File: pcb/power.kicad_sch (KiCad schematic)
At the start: 38 parts, among them U10 TPS541620

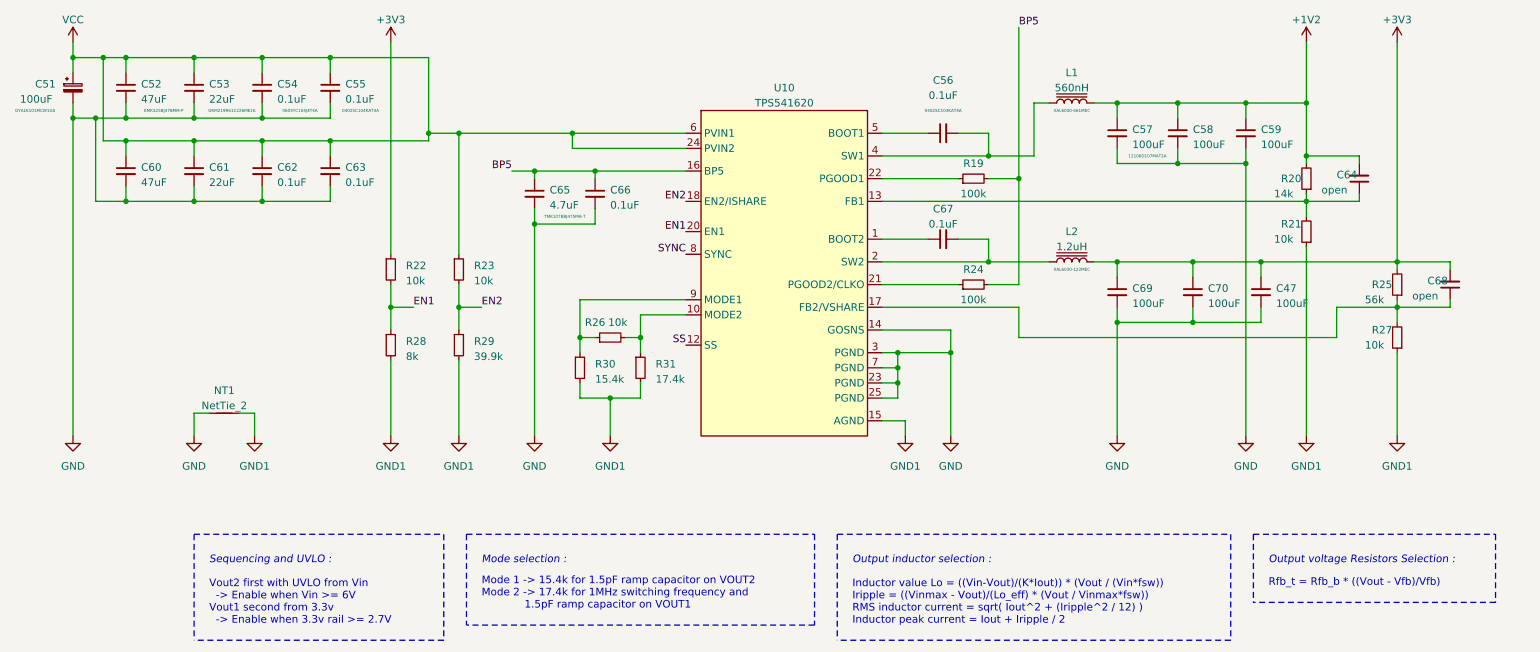
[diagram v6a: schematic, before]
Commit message: change to lx9 and reduce power
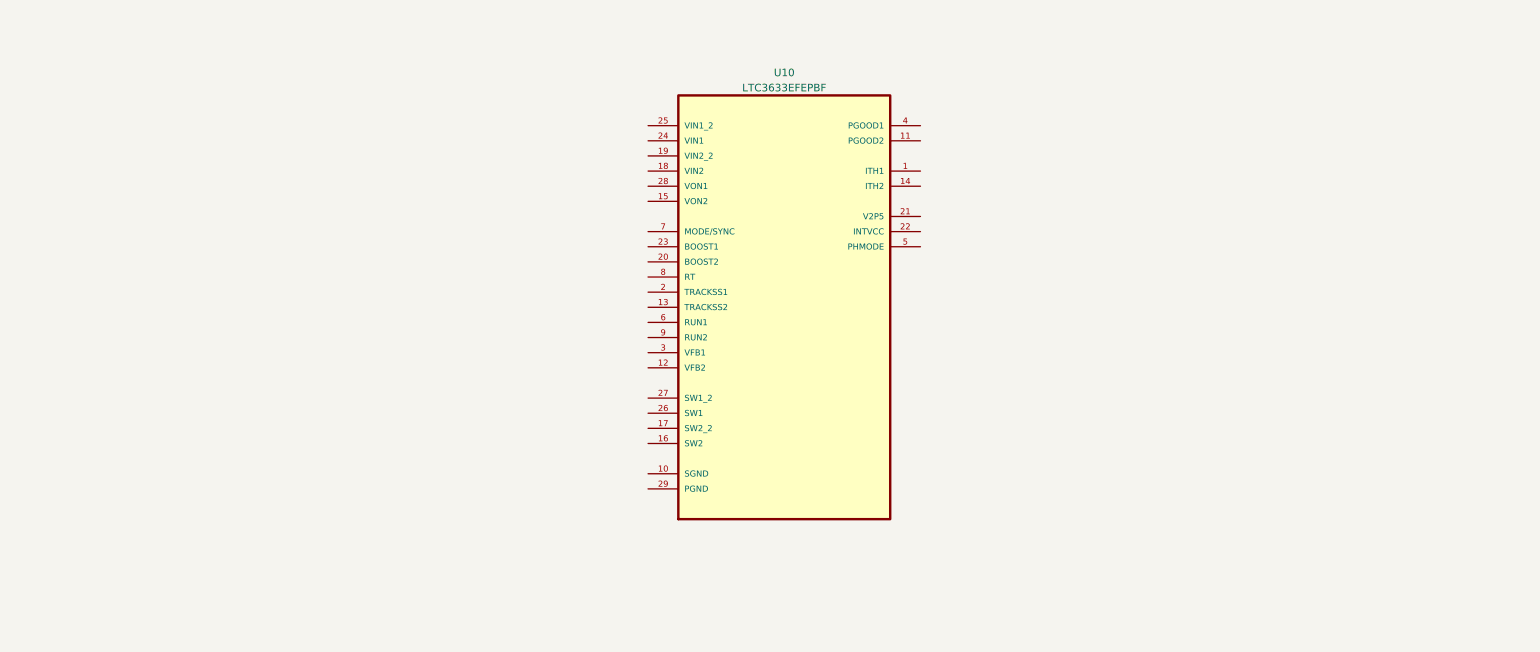
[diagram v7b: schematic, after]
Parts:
- removed C47, C57, C58, C59, C69, C70: 100uF, Capacitor_SMD:C_1210_3225Metric, symbol Device:C_Small
- removed C51: 100uF, Capacitor_SMD:CP_Elec_6.3x7.7, symbol Device:C_Polarized_Small
- removed C52, C60: 47uF, Capacitor_SMD:C_1210_3225Metric, symbol Device:C_Small
- removed C53, C61: 22uF, Capacitor_SMD:C_0805_2012Metric, symbol Device:C_Small
- removed C54, C62: 0.1uF, Capacitor_SMD:C_0603_1608Metric, symbol Device:C_Small
- removed C55, C56, C63, C66, C67: 0.1uF, Capacitor_SMD:C_0402_1005Metric, symbol Device:C_Small
- removed C64, C68: open, Capacitor_SMD:C_0402_1005Metric, symbol Device:C_Small
- removed C65: 4.7uF, Capacitor_SMD:C_0603_1608Metric, symbol Device:C_Small
- removed L1: 560nH, XAL6030-561MEB:IND_XAL6030-561MEB, symbol Device:L_Iron
- removed L2: 1.2uH, XAL6030-122MEB:IND_XAL6030-122MEB, symbol Device:L_Iron
- removed NT1: NetTie_2, NetTie:NetTie-2_SMD_Pad0.5mm, symbol Device:NetTie_2
- removed R19, R24: 100k, Resistor_SMD:R_0402_1005Metric, symbol Device:R_Small
- removed R20: 14k, Resistor_SMD:R_0402_1005Metric, symbol Device:R_Small
- removed R21, R22, R23, R26, R27: 10k, Resistor_SMD:R_0402_1005Metric, symbol Device:R_Small
- removed R25: 56k, Resistor_SMD:R_0402_1005Metric, symbol Device:R_Small
- removed R28: 8k, Resistor_SMD:R_0402_1005Metric, symbol Device:R_Small
- removed R29: 39.9k, Resistor_SMD:R_0402_1005Metric, symbol Device:R_Small
- removed R30: 15.4k, Resistor_SMD:R_0402_1005Metric, symbol Device:R_Small
- removed R31: 17.4k, Resistor_SMD:R_0402_1005Metric, symbol Device:R_Small
- removed U10: TPS541620, TPS541620:TPS541620, symbol Regulator_Switching:TPS541620
- added U10: LTC3633EFEPBF, SOP65P640X120-29N, symbol LTC3633EFEPBF:LTC3633EFEPBF
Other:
- note removed: "Inductor value Lo = ((Vin-Vout)/(K*Iout)) * (Vout / (Vin*fsw)) Iripple = ((Vinmax - Vout)/(Lo_eff) * (Vout / Vinmax*fsw)) RMS inductor current = sqrt( Iout^2 + (Iripple^2 / 12) ) Inductor peak current = Iout + Iripple / 2"
- note removed: "Mode 1 -> 15.4k for 1.5pF ramp capacitor on VOUT2 Mode 2 -> 17.4k for 1MHz switching frequency and 1.5pF ramp capacitor on VOUT1"
- note removed: "Mode selection :"
- note removed: "Output inductor selection :"
- note removed: "Output voltage Resistors Selection :"
- note removed: "Rfb_t = Rfb_b * ((Vout - Vfb)/Vfb)"
- note removed: "Sequencing and UVLO :"
- note removed: "Vout2 first with UVLO from Vin -> Enable when Vin >= 6V Vout1 second from 3.3v -> Enable when 3.3v rail >= 2.7V"

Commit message: route pol
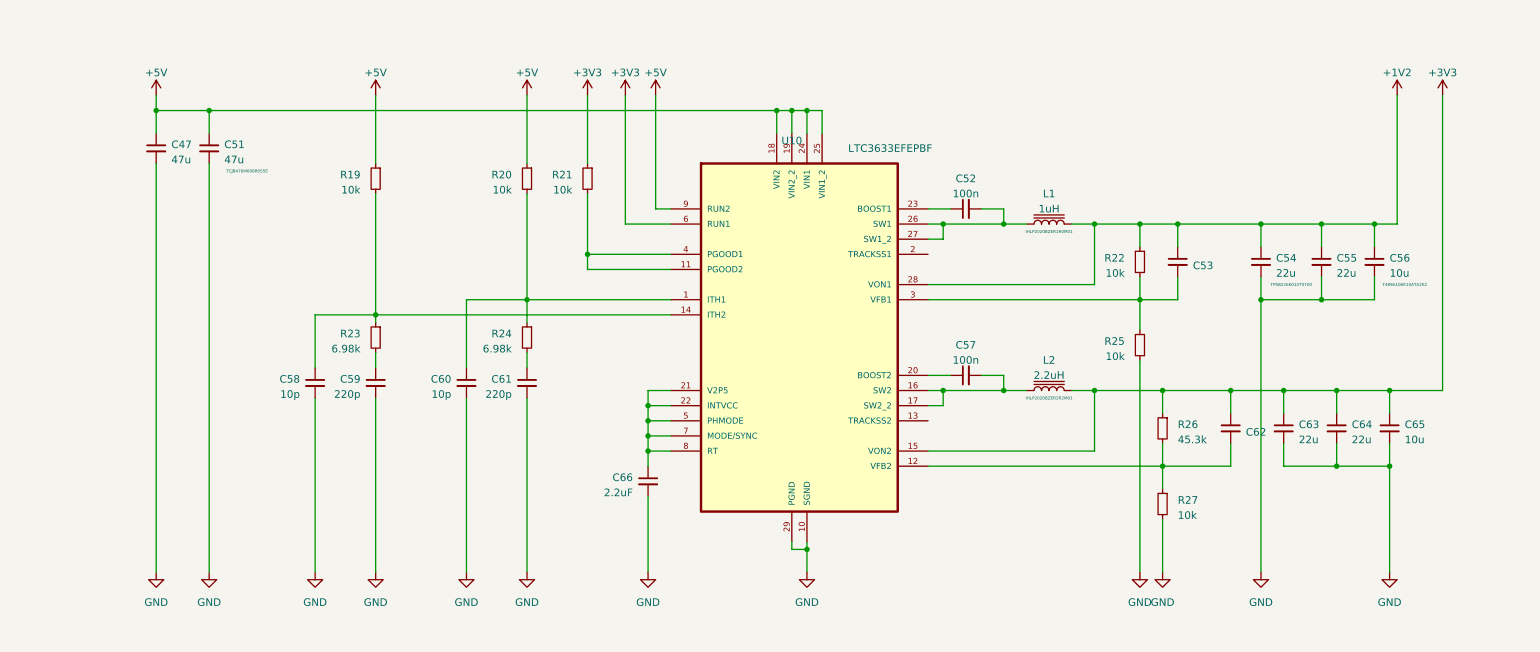
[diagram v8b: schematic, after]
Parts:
- added C47, C51: 47u, Capacitor_SMD:C_1210_3225Metric, symbol Device:C_Small
- added C52, C57: 100n, Capacitor_SMD:C_0402_1005Metric, symbol Device:C_Small
- added C53, C62: NL, Capacitor_SMD:C_0603_1608Metric, symbol Device:C_Small
- added C54, C55, C63, C64: 22u, Capacitor_SMD:C_1206_3216Metric, symbol Device:C_Small
- added C56, C65: 10u, Capacitor_SMD:C_1206_3216Metric, symbol Device:C_Small
- added C58, C60: 10p, Capacitor_SMD:C_0402_1005Metric, symbol Device:C_Small
- added C59, C61: 220p, Capacitor_SMD:C_0402_1005Metric, symbol Device:C_Small
- added C66: 2.2uF, Capacitor_SMD:C_0603_1608Metric, symbol Device:C_Small
- added L1: 1uH, 2020_5252_Inductor:IND_#A915BY-100M=P3, symbol Device:L_Iron
- added L2: 2.2uH, 2020_5252_Inductor:IND_#A915BY-100M=P3, symbol Device:L_Iron
- added R19, R20, R21, R22, R25, R27: 10k, Resistor_SMD:R_0402_1005Metric, symbol Device:R_Small
- added R23, R24: 6.98k, Resistor_SMD:R_0402_1005Metric, symbol Device:R_Small
- added R26: 45.3k, Resistor_SMD:R_0402_1005Metric, symbol Device:R_Small
- U10: footprint SOP65P640X120-29N -> SOP65P640X120-29N:SOP65P640X120-29N
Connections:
- net at U10.1 (ITH1): now also C60.1, R20.2, R24.1
- net GND: now reaches U10.10 (SGND)
- net GND: now also U10.29 (PGND), C47.2, C51.2, C54.2, C55.2, C56.2, C58.2, C59.2, C60.2, C61.2, C63.2, C64.2, C65.2, C66.2, R25.2, R27.2
- net at U10.11 (PGOOD2): now also U10.4 (PGOOD1), R21.2
- net at U10.12 (VFB2): now also C62.2, R26.2, R27.1
- net at U10.14 (ITH2): now also C58.1, R19.2, R23.1
- net +3V3: now reaches U10.15 (VON2)
- net +3V3: now also U10.6 (RUN1), C62.1, C63.1, C64.1, C65.1, L2.2, R21.1, R26.1
- net at U10.16 (SW2): now also U10.17 (SW2_2), C57.2, L2.1
- net +5V: now reaches U10.18 (VIN2)
- net +5V: now also U10.19 (VIN2_2), U10.24 (VIN1), U10.25 (VIN1_2), U10.9 (RUN2), C47.1, C51.1, R19.1, R20.1
- net at U10.20 (BOOST2): now also C57.1
- net at U10.21 (V2P5): now also U10.22 (INTVCC), U10.5 (PHMODE), U10.7 (MODE/SYNC), U10.8 (RT), C66.1
- net at U10.23 (BOOST1): now also C52.1
- net at U10.26 (SW1): now also U10.27 (SW1_2), C52.2, L1.1
- net +1V2: now reaches U10.28 (VON1)
- net +1V2: now also C53.1, C54.1, C55.1, C56.1, L1.2, R22.1
- net at U10.3 (VFB1): now also C53.2, R22.2, R25.1
- new net: C59.1, R23.2
- new net: C61.1, R24.2
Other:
- moved on the sheet: U10
